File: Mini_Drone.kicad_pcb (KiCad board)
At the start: 4 copper layers, 55.5 x 48.3 mm, 75 parts, among them J1 Conn_01x02, J3 Conn_01x02, J4 Conn_01x06, J7 Conn_01x11, J8 Conn_01x11, Q1 AO3400A, Q2 AO3400A, Q3 AO3400A, Q4 AO3400A, U1 ESP32-S3-WROOM-1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

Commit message: Almost finished need to check it before the ordering need check all the violaition
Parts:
- removed the REF** at (225.7, 105.2)
- removed the REF** at (211.0, 105.2)
- removed the REF** at (240.0, 105.2)
- removed the REF** at (197.6, 105.2)
- removed S2: TL1105F160Q, Mini_Drone_prj:SW_TL1105F160Q
- added REF**: MouseBite-Part_2.0x2.0mm_inset_D0.5mm_P0.85mm_5h, Panelization:MouseBite-Part_2.0x2.0mm_inset_D0.5mm_P0.85mm_5h, F.Cu at (210.9, 107.0)
- added REF**: MouseBite-Part_2.0x2.0mm_inset_D0.5mm_P0.85mm_5h, Panelization:MouseBite-Part_2.0x2.0mm_inset_D0.5mm_P0.85mm_5h, F.Cu at (239.9, 107.0)
- added REF**: MouseBite-Part_2.0x2.0mm_inset_D0.5mm_P0.85mm_5h, Panelization:MouseBite-Part_2.0x2.0mm_inset_D0.5mm_P0.85mm_5h, F.Cu at (225.5, 107.0)
- added REF**: MouseBite-Part_2.0x2.0mm_inset_D0.5mm_P0.85mm_5h, Panelization:MouseBite-Part_2.0x2.0mm_inset_D0.5mm_P0.85mm_5h, F.Cu at (197.5, 107.0)
- S3: value 100SP1T1B4M2QE -> TL1105F160Q; footprint Mini_Drone_prj:SW_100SP1T1B4M2QE -> Mini_Drone_prj:SW_TL1105F160Q
- moved S3 59.2 mm to (195.6, 100.0), turned to 180 degrees
- moved C1 1.73 mm to (227.5, 117.8)
- moved C4 1.73 mm to (212.5, 117.8)
- moved C5 1.73 mm to (199.3, 117.7)
- moved C6 1.73 mm to (242.0, 117.8)
- moved D2 1.73 mm to (227.5, 113.7)
- moved D3 1.73 mm to (212.9, 114.6)
- moved D4 1.73 mm to (241.9, 114.4)
- moved D6 1.73 mm to (199.5, 113.9)
- moved Q1 1.73 mm to (193.7, 115.1)
- moved Q2 1.73 mm to (221.9, 115.2)
- moved Q3 1.73 mm to (207.2, 115.6)
- moved Q4 1.73 mm to (236.4, 115.2)
- moved R4 1.73 mm to (194.2, 112.0)
- moved R5 1.73 mm to (222.1, 112.0)
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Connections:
- Q2 pad 2: unconnected-(Q2-S-Pad2) -> Net-(Q2-S)
- Q3 pad 2: unconnected-(Q3-S-Pad2) -> Net-(Q3-S)
- Q4 pad 2: unconnected-(Q4-S-Pad2) -> Net-(Q4-S)
- R5 pad 2: Net-(R5-Pad2) -> Net-(Q2-S)
- R6 pad 2: Net-(R6-Pad2) -> Net-(Q3-S)
- R7 pad 2: Net-(R7-Pad2) -> Net-(Q4-S)
- S3 pad 1: /BAT+ -> /EN
- S3 pad 2: /BAT+ -> /EN
- S3 pad 3: unconnected-(S3-Pad3) -> GND
- TP12 pad 1: Net-(R6-Pad2) -> Net-(Q3-S)
- TP17 pad 1: Net-(R7-Pad2) -> Net-(Q4-S)
- TP4 pad 1: Net-(R5-Pad2) -> Net-(Q2-S)
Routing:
- net (no net): track 13.3 -> 0.00 mm
- net Net-(Q3-S): track 0.00 -> 4.60 mm
- net Net-(Q2-S): track 0.00 -> 4.37 mm
- net Net-(Q4-S): track 0.00 -> 4.32 mm
- net Net-(D2-A): track 10.5 -> 12.3 mm
- net Net-(D6-A): track 11.3 -> 12.6 mm
- net /EN: track 83.4 -> 82.6 mm
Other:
- board size 55.5 x 48.3 mm -> 55 x 50.7 mm

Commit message: Hari version switchled
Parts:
- added D8: LED, LED_SMD:LED_0603_1608Metric, F.Cu at (202.5, 101.2)
- added D9: LED, LED_SMD:LED_0603_1608Metric, F.Cu at (196.7, 93.8)
- added R10: 220, Resistor_SMD:R_0603_1608Metric, F.Cu at (206.5, 101.2)
- added R11: 220, Resistor_SMD:R_0603_1608Metric, F.Cu at (199.1, 93.9)
- added S2: 500SSP1S1M2REA, Mini_Drone_prj:SW_500SSP1S1M2REA, F.Cu at (215.0, 103.0)
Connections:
- U3 pad 3: /BAT+ -> Net-(U3-EN)
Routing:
- net /BAT+: track 28.1 -> 36.5 mm
- net Net-(D9-A): track 0.00 -> 2.43 mm
- net Net-(D8-A): track 0.00 -> 2.41 mm
- net +3V3: track 82.5 -> 84.7 mm

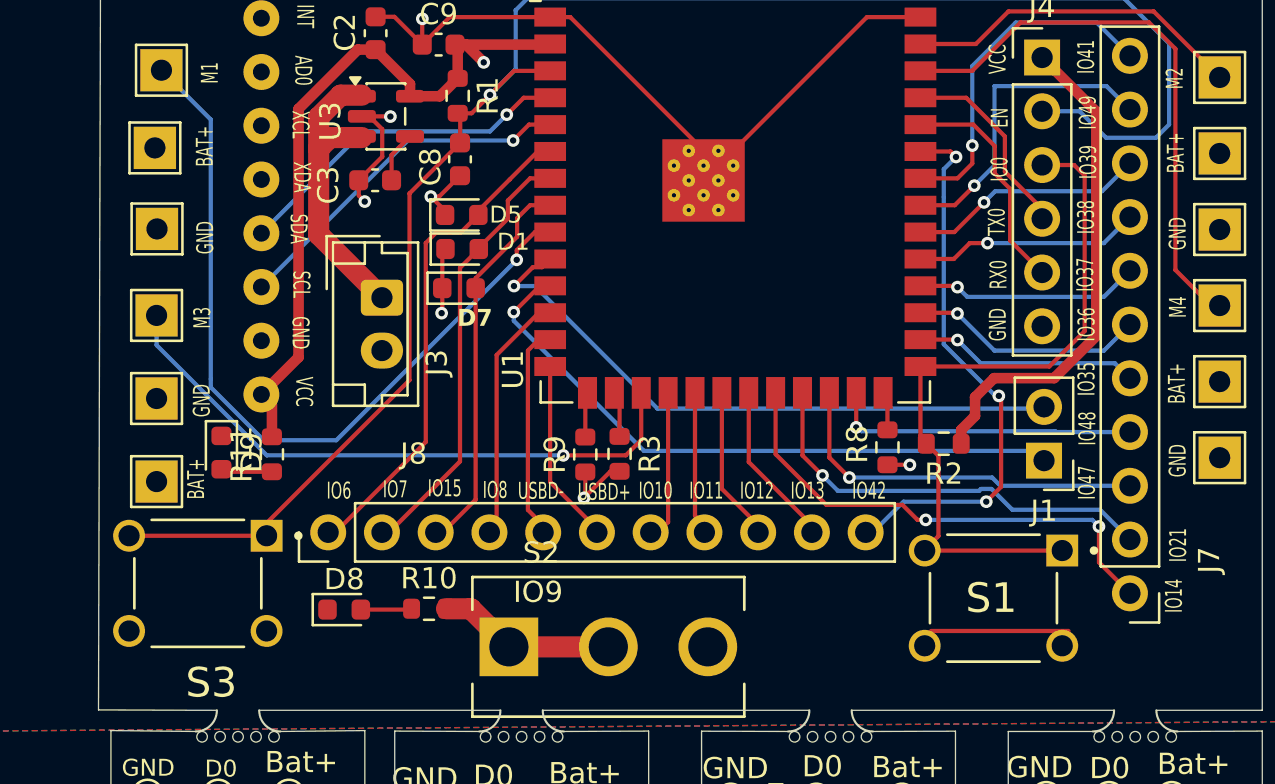
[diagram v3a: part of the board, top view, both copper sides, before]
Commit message: needs to increase the outline
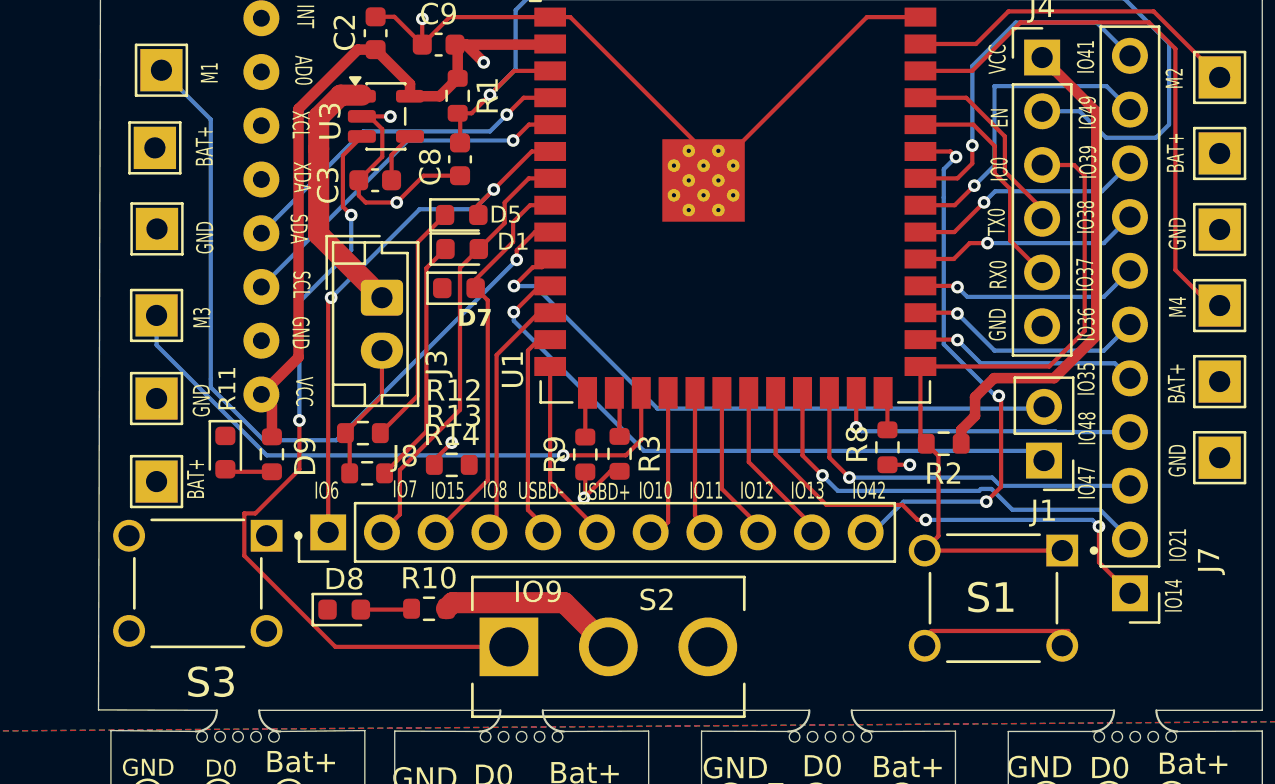
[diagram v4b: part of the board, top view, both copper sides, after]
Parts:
- added R12: 220, Resistor_SMD:R_0603_1608Metric, F.Cu at (203.4, 92.9)
- added R13: 220, Resistor_SMD:R_0603_1608Metric, F.Cu at (203.6, 94.8)
- added R14: 220, Resistor_SMD:R_0603_1608Metric, F.Cu at (207.6, 94.4)
- moved D9 0.19 mm to (196.9, 93.8)
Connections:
- D1 pad 1: GND -> Net-(D1-K)
- D5 pad 1: GND -> Net-(D5-K)
- D7 pad 1: GND -> Net-(D7-K)
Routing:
- net Net-(U3-EN): track 0.00 -> 38.2 mm, vias 0 -> 2
- net /EN: track 82.6 -> 53.8 mm
- net Net-(D1-K): track 0.00 -> 11.8 mm
- net Net-(D5-K): track 0.00 -> 11.4 mm
- net GND: track 58.9 -> 65.9 mm, vias 7 -> 6
- net /LED1: track 23.3 -> 25.9 mm, vias 0 -> 2
- net /BAT+: track 36.5 -> 34.5 mm
- net /LED3: track 18.1 -> 18.7 mm

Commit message: final checking and then order
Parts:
- removed R10, R13, R14: 220, Resistor_SMD:R_0603_1608Metric
- added R15: 220, Resistor_SMD:R_0603_1608Metric, F.Cu at (207.6, 94.3)
- added R16: 220, Resistor_SMD:R_0603_1608Metric, F.Cu at (203.7, 94.7)
- added R17: 220, Resistor_SMD:R_0603_1608Metric, F.Cu at (203.5, 92.9)
- S2: footprint Mini_Drone_prj:SW_500SSP1S1M2REA -> Mini_Drone_prj:slide swithc
- moved R12 8.90 mm to (206.3, 101.3), turned to 180 degrees
- moved S2 0.64 mm to (215.3, 102.4)
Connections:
- R12 pad 1: GND -> /BAT+
- R12 pad 2: Net-(D5-K) -> Net-(D8-A)
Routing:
- net Net-(D7-K): track 0.00 -> 8.94 mm, vias 0 -> 2
- net /BAT+: track 34.5 -> 35.7 mm

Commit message: added gnd to the switch other terminal
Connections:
- S2 pad 3: unconnected-(S2-Pad3) -> GND
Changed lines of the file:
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@@
 	(net 62 "Net-(D8-A)")
 	(net 63 "Net-(D9-A)")
-	(net 64 "unconnected-(S2-Pad3)")
-	(net 65 "Net-(U3-EN)")
-	(net 66 "Net-(D1-K)")
-	(net 67 "Net-(D5-K)")
-	(net 68 "Net-(D7-K)")
+	(net 64 "Net-(U3-EN)")
+	(net 65 "Net-(D1-K)")
+	(net 66 "Net-(D5-K)")
+	(net 67 "Net-(D7-K)")
 	(footprint "TestPoint:TestPoint_Pad_D1.0mm"
 		(layer "F.Cu")
@@
 			(layers "F.Cu" "F.Mask" "F.Paste")
 			(roundrect_rratio 0.25)
-			(net 65 "Net-(U3-EN)")
+			(net 64 "Net-(U3-EN)")
 			(pinfunction "EN")
 			(pintype "input")
@@
 			(layers "F.Cu" "F.Mask" "F.Paste")
 			(roundrect_rratio 0.25)
-			(net 67 "Net-(D5-K)")
+			(net 66 "Net-(D5-K)")
 			(pintype "passive")
 		)
@@
 			(layers "F.Cu" "F.Mask" "F.Paste")
 			(roundrect_rratio 0.25)
-			(net 68 "Net-(D7-K)")
+			(net 67 "Net-(D7-K)")
 			(pinfunction "K")
 			(pintype "passive")
@@
 			(layers "*.Cu" "*.Mask")
 			(remove_unused_layers no)
-			(net 65 "Net-(U3-EN)")
+			(net 64 "Net-(U3-EN)")
 			(pintype "passive")
 			(solder_mask_margin 0.0508)
@@
 			(layers "*.Cu" "*.Mask")
 			(remove_unused_layers no)
-			(net 64 "unconnected-(S2-Pad3)")
-			(pintype "passive+no_connect")
+			(net 2 "GND")
+			(pintype "passive")
 			(solder_mask_margin 0.0508)
 			(solder_paste_margin 0)
@@
 			(layers "F.Cu" "F.Mask" "F.Paste")
 			(roundrect_rratio 0.25)
-			(net 66 "Net-(D1-K)")
+			(net 65 "Net-(D1-K)")
 			(pinfunction "K")
 			(pintype "passive")
@@
 			(layers "F.Cu" "F.Mask" "F.Paste")
 			(roundrect_rratio 0.25)
-			(net 68 "Net-(D7-K)")
+			(net 67 "Net-(D7-K)")
 			(pintype "passive")
 		)
@@
 			(layers "F.Cu" "F.Mask" "F.Paste")
 			(roundrect_rratio 0.25)
-			(net 66 "Net-(D1-K)")
+			(net 65 "Net-(D1-K)")
 			(pintype "passive")
 		)
@@
 			(layers "F.Cu" "F.Mask" "F.Paste")
 			(roundrect_rratio 0.25)
-			(net 67 "Net-(D5-K)")
+			(net 66 "Net-(D5-K)")
 			(pinfunction "K")
 			(pintype "passive")
@@
 		(width 0.2)
 		(layer "F.Cu")
-		(net 65)
+		(net 64)
 	)
 	(segment
@@
 		(width 0.2)
 		(layer "F.Cu")
-		(net 65)
+		(net 64)
 	)
 	(segment
@@
 		(width 0.2)
 		(layer "F.Cu")
-		(net 65)
+		(net 64)
 	)
 	(segment
@@
 		(width 0.2)
 		(layer "F.Cu")
-		(net 65)
+		(net 64)
 	)
 	(segment
@@
 		(width 0.2)
 		(layer "F.Cu")
-		(net 65)
+		(net 64)
 	)
 	(segment
@@
 		(width 0.2)
 		(layer "F.Cu")
-		(net 65)
+		(net 64)
 	)
 	(segment
@@
 		(width 0.2)
 		(layer "F.Cu")
-		(net 65)
+		(net 64)
 	)
 	(segment
@@
 		(width 0.2)
 		(layer "F.Cu")
-		(net 65)
+		(net 64)
 	)
 	(segment
@@
 		(width 0.2)
 		(layer "F.Cu")
-		(net 65)
+		(net 64)
 	)
 	(segment
@@
 		(width 0.2)
 		(layer "F.Cu")
-		(net 65)
+		(net 64)
 	)
 	(via
@@
 		(drill 0.3)
 		(layers "F.Cu" "B.Cu")
-		(net 65)
+		(net 64)
 	)
 	(via
@@
 		(drill 0.3)
 		(layers "F.Cu" "B.Cu")
-		(net 65)
+		(net 64)
 	)
 	(segment
@@
 		(width 0.2)
 		(layer "B.Cu")
-		(net 65)
+		(net 64)
 	)
 	(segment
@@
 		(width 0.2)
 		(layer "B.Cu")
-		(net 65)
+		(net 64)
 	)
 	(segment
@@
 		(width 0.2)
 		(layer "B.Cu")
-		(net 65)
+		(net 64)
 	)
 	(segment
@@
 		(width 0.2)
 		(layer "F.Cu")
-		(net 66)
+		(net 65)
 	)
 	(segment
@@
 		(width 0.2)
 		(layer "F.Cu")
-		(net 66)
+		(net 65)
 	)
 	(segment
@@
 		(width 0.2)
 		(layer "F.Cu")
-		(net 66)
+		(net 65)
 	)
 	(segment
@@
 		(width 0.2)
 		(layer "F.Cu")
-		(net 67)
+		(net 66)
 	)
 	(segment
@@
 		(width 0.2)
 		(layer "F.Cu")
-		(net 67)
+		(net 66)
 	)
 	(segment
@@
 		(width 0.2)
 		(layer "F.Cu")
-		(net 67)
+		(net 66)
 	)
 	(segment
@@
 		(width 0.2)
 		(layer "F.Cu")
-		(net 67)
+		(net 66)
 	)
 	(segment
@@
 		(width 0.2)
 		(layer "F.Cu")
-		(net 68)
+		(net 67)
 	)
 	(segment
@@
 		(width 0.2)
 		(layer "F.Cu")
-		(net 68)
+		(net 67)
 	)
 	(segment
@@
 		(width 0.2)
 		(layer "F.Cu")
-		(net 68)
+		(net 67)
 	)
 	(segment
@@
 		(width 0.2)
 		(layer "F.Cu")
-		(net 68)
+		(net 67)
 	)
 	(via
@@
 		(drill 0.3)
 		(layers "F.Cu" "B.Cu")
-		(net 68)
+		(net 67)
 	)
 	(via
@@
 		(drill 0.3)
 		(layers "F.Cu" "B.Cu")
-		(net 68)
+		(net 67)
 	)
 	(segment
@@
 		(width 0.2)
 		(layer "B.Cu")
-		(net 68)
+		(net 67)
 	)
 	(segment
@@
 		(width 0.2)
 		(layer "B.Cu")
-		(net 68)
+		(net 67)
 	)
 	(zone

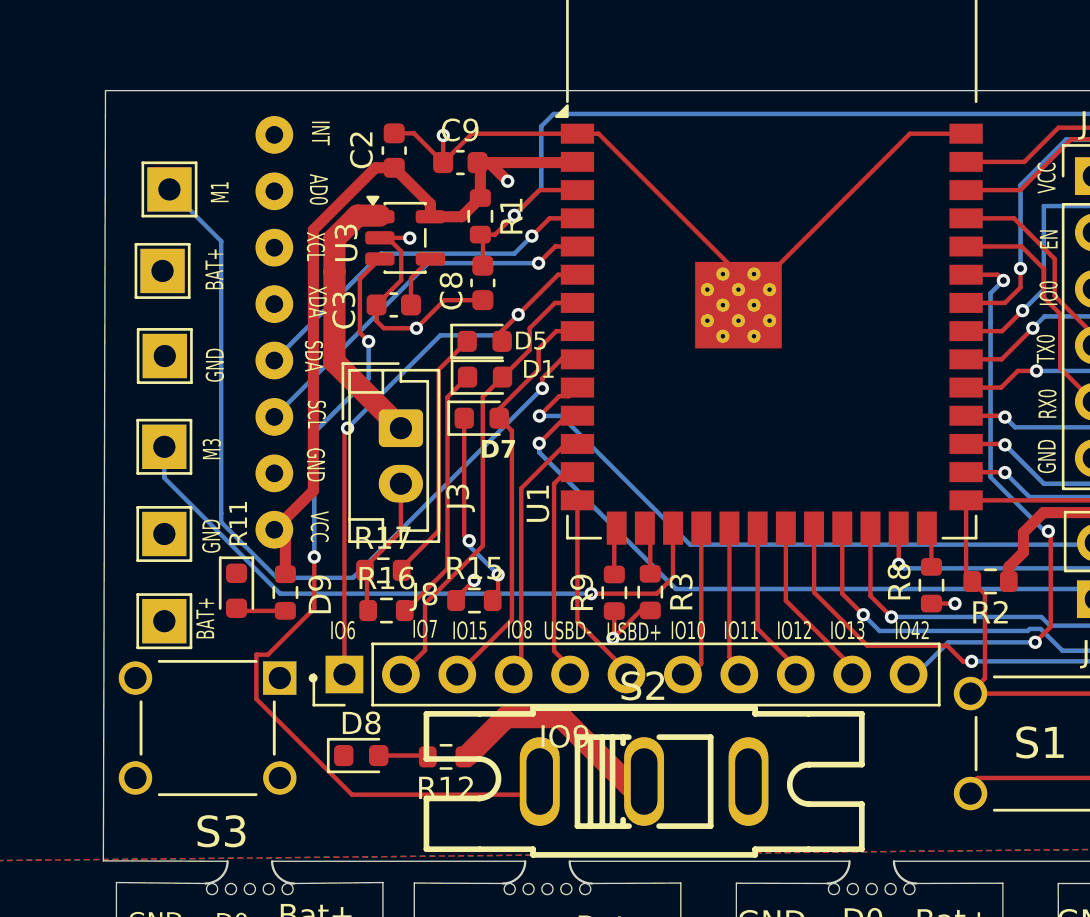
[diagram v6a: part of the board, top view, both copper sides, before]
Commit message: rectified the unconnected gnd net need to again check everything before ordering once more
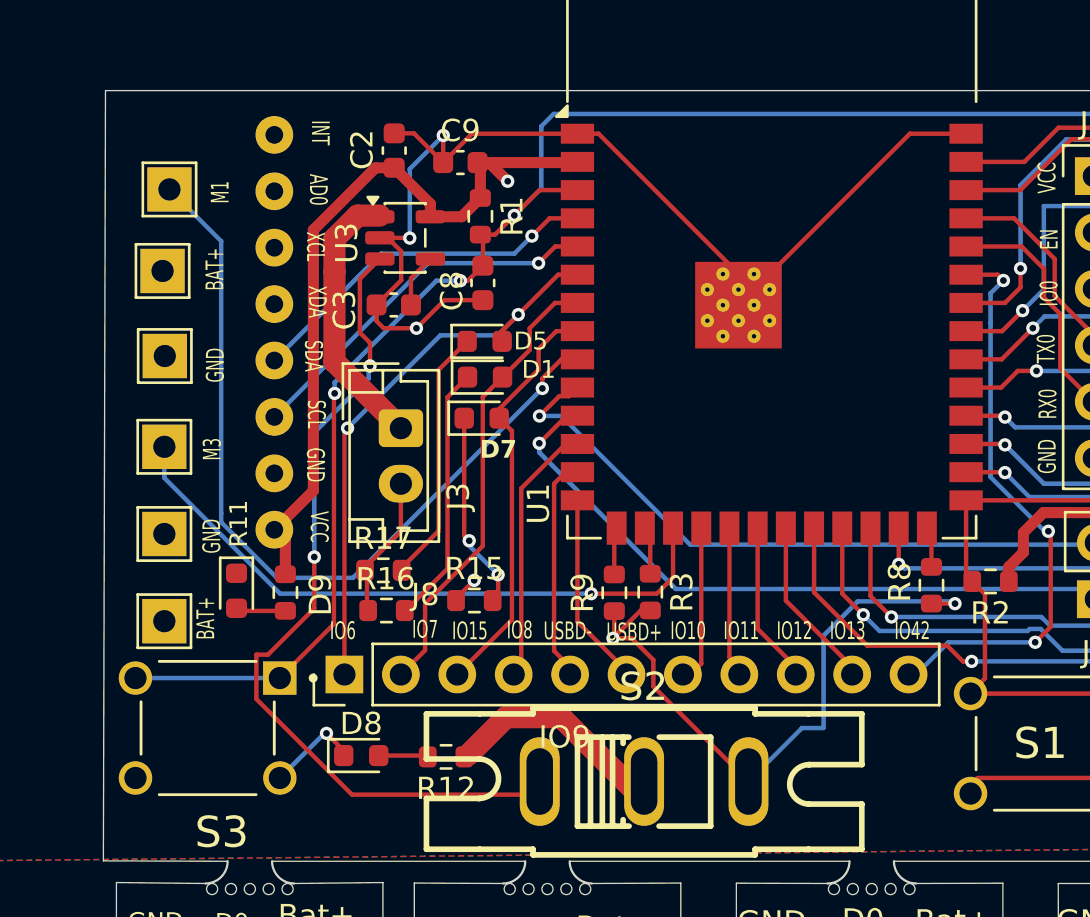
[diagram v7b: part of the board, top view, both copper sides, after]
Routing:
- net GND: track 65.9 -> 100.0 mm, vias 6 -> 7
- net /EN: track 53.8 -> 83.5 mm, vias 1 -> 3
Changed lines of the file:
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@@
 		(tags "resistor")
 		(property "Reference" "R16"
-			(at 0 -1.43 0)
+			(at -0.04 -1.42 0)
 			(layer "F.SilkS")
 			(effects
@@
 	)
 	(segment
+		(start 215.67 96.93424)
+		(end 215.67 98.13)
+		(width 0.2)
+		(layer "F.Cu")
+		(net 2)
+	)
+	(segment
 		(start 206.775 94.175)
 		(end 207.6 93.35)
@@
 	)
 	(segment
+		(start 213.85 95.96)
+		(end 214.69576 95.96)
+		(width 0.2)
+		(layer "F.Cu")
+		(net 2)
+	)
+	(segment
 		(start 215.53 94.705)
 		(end 215.105 94.705)
@@
 	)
 	(segment
+		(start 214.69576 95.96)
+		(end 215.67 96.93424)
+		(width 0.2)
+		(layer "F.Cu")
+		(net 2)
+	)
+	(segment
+		(start 201.7275 101.0175)
+		(end 200.95 100.24)
+		(width 0.2)
+		(layer "F.Cu")
+		(net 2)
+	)
+	(segment
 		(start 207.505 73.24)
 		(end 212.25 73.24)
@@
 	)
 	(segment
+		(start 201.7275 101.24)
+		(end 201.7275 101.0175)
+		(width 0.2)
+		(layer "F.Cu")
+		(net 2)
+	)
+	(segment
 		(start 204.316 79.839)
 		(end 203.205 80.95)
@@
 	)
 	(segment
+		(start 215.67 98.13)
+		(end 219.95 102.41)
+		(width 0.2)
+		(layer "F.Cu")
+		(net 2)
+	)
+	(segment
 		(start 204.3 91.15)
 		(end 204.3 89)
@@
 	)
 	(via
+		(at 200.95 100.24)
+		(size 0.6)
+		(drill 0.3)
+		(layers "F.Cu" "B.Cu")
+		(net 2)
+	)
+	(via
 		(at 213.85 95.96)
 		(size 0.6)
@@
 	)
 	(segment
+		(start 200.95 100.24)
+		(end 200.86 100.24)
+		(width 0.2)
+		(layer "B.Cu")
+		(net 2)
+	)
+	(segment
+		(start 222.36 100)
+		(end 219.95 102.41)
+		(width 0.2)
+		(layer "B.Cu")
+		(net 2)
+	)
+	(segment
+		(start 229.25 94.4)
+		(end 229.149 94.299)
+		(width 0.2)
+		(layer "B.Cu")
+		(net 2)
+	)
+	(segment
+		(start 223.33 95.840057)
+		(end 223.33 100)
+		(width 0.2)
+		(layer "B.Cu")
+		(net 2)
+	)
+	(segment
+		(start 204.7 74.83)
+		(end 206.21 73.32)
+		(width 0.2)
+		(layer "B.Cu")
+		(net 2)
+	)
+	(segment
+		(start 229.149 94.299)
+		(end 224.871057 94.299)
+		(width 0.2)
+		(layer "B.Cu")
+		(net 2)
+	)
+	(segment
+		(start 224.871057 94.299)
+		(end 223.33 95.840057)
+		(width 0.2)
+		(layer "B.Cu")
+		(net 2)
+	)
+	(segment
+		(start 223.33 100)
+		(end 222.36 100)
+		(width 0.2)
+		(layer "B.Cu")
+		(net 2)
+	)
+	(segment
+		(start 204.7 77.94)
+		(end 204.7 74.83)
+		(width 0.2)
+		(layer "B.Cu")
+		(net 2)
+	)
+	(segment
+		(start 200.86 100.24)
+		(end 198.85 102.25)
+		(width 0.2)
+		(layer "B.Cu")
+		(net 2)
+	)
+	(segment
 		(start 235.5 82.3029)
 		(end 235.5 82.77)
@@
 	)
 	(segment
+		(start 201.285735 95.314265)
+		(end 201.285735 84.965735)
+		(width 0.2)
+		(layer "F.Cu")
+		(net 12)
+	)
+	(segment
+		(start 207.315 79.86)
+		(end 207.99 79.185)
+		(width 0.2)
+		(layer "F.Cu")
+		(net 12)
+	)
+	(segment
 		(start 212.25 75.78)
 		(end 210.545 75.78)
@@
 	)
 	(segment
+		(start 206.98 79.86)
+		(end 207.315 79.86)
+		(width 0.2)
+		(layer "F.Cu")
+		(net 12)
+	)
+	(segment
 		(start 208 77.905)
 		(end 208 79.175)
@@
 		(net 12)
 	)
+	(segment
+		(start 198.85 97.75)
+		(end 201.285735 95.314265)
+		(width 0.2)
+		(layer "F.Cu")
+		(net 12)
+	)
+	(segment
+		(start 201.285735 84.965735)
+		(end 201.318628 84.932842)
+		(width 0.2)
+		(layer "F.Cu")
+		(net 12)
+	)
+	(via
+		(at 206.98 79.86)
+		(size 0.6)
+		(drill 0.3)
+		(layers "F.Cu" "B.Cu")
+		(net 12)
+	)
+	(via
+		(at 201.318628 84.932842)
+		(size 0.6)
+		(drill 0.3)
+		(layers "F.Cu" "B.Cu")
+		(net 12)
+	)
 	(via
 		(at 209.4075 76.9175)
@@
 	)
 	(segment
+		(start 201.318628 84.440194)
+		(end 205.898822 79.86)
+		(width 0.2)
+		(layer "B.Cu")
+		(net 12)
+	)
+	(segment
 		(start 211.18 72.35)
 		(end 239.37 72.35)
@@
 	)
 	(segment
+		(start 192.35 97.75)
+		(end 198.85 97.75)
+		(width 0.2)
+		(layer "B.Cu")
+		(net 12)
+	)
+	(segment
 		(start 239.37 72.35)
 		(end 241.5 74.48)
@@
 	)
 	(segment
+		(start 205.898822 79.86)
+		(end 206.98 79.86)
+		(width 0.2)
+		(layer "B.Cu")
+		(net 12)
+	)
+	(segment
 		(start 238.52 78.94)
 		(end 237.27 77.69)
@@
 	)
 	(segment
+		(start 201.318628 84.932842)
+		(end 201.318628 84.440194)
+		(width 0.2)
+		(layer "B.Cu")
+		(net 12)
+	)
+	(segment
 		(start 205.08875 79.41875)
 		(end 205.6275 78.88)
@@
 	)
 	(segment
+		(start 202.454 79.7785)
+		(end 203.3525 78.88)
+		(width 0.2)
+		(layer "F.Cu")
+		(net 64)
+	)
+	(segment
 		(start 202.1 103)
 		(end 197.795 98.695)
@@
 	)
 	(segment
-		(start 210.3 101.8)
-		(end 210.3 103)
+		(start 202.91149 83.697275)
+		(end 202.91149 82.65749)
 		(width 0.2)
 		(layer "F.Cu")
@@
 	)
 	(segment
-		(start 202.454 82.2)
-		(end 202.454 79.7785)
+		(start 210.3 101.8)
+		(end 210.3 103)
 		(width 0.2)
 		(layer "F.Cu")
@@
 	)
 	(segment
-		(start 202.848765 82.594765)
+		(start 202.91149 82.65749)
 		(end 202.454 82.2)
 		(width 0.2)
@@
 	)
 	(segment
+		(start 202.454 82.2)
+		(end 202.454 79.7785)
+		(width 0.2)
+		(layer "F.Cu")
+		(net 64)
+	)
+	(segment
 		(start 198.319064 96.695)
 		(end 200.4 94.614064)
@@
 		(net 64)
 	)
-	(segment
-		(start 202.454 79.7785)
-		(end 203.3525 78.88)
-		(width 0.2)
-		(layer "F.Cu")
-		(net 64)
-	)
 	(via
 		(at 200.4 92.3)
@@
 	)
 	(via
-		(at 202.848765 82.594765)
+		(at 202.91149 83.697275)
 		(size 0.6)
 		(drill 0.3)
@@
 	)
 	(segment
-		(start 200.4 86.7)
-		(end 200.4 92.3)
+		(start 202.91149 83.697275)
+		(end 202.848765 83.76)
 		(width 0.2)
 		(layer "B.Cu")
@@
 	)
 	(segment
-		(start 202.848765 82.594765)
+		(start 202.848765 83.76)
 		(end 202.848765 84.251235)
 		(width 0.2)
 		(layer "B.Cu")
+		(net 64)
+	)
+	(segment
+		(start 200.4 86.7)
+		(end 200.4 92.3)
+		(width 0.2)
+		(layer "B.Cu")
